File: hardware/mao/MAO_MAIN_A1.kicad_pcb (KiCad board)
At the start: 4 copper layers, 58 x 56 mm, 137 parts, among them J101 USB-C, J102 BAT, J201 TAG, J301 LCD, J501 LRA, Q101 AO3401A, Q302 DMG2302UK, Q501 AO3400A, SW301 SKQGADE010, U101 TPD2E2U06, U102 BQ25185DLHR, U103 MAX17048G+T10, U104 TPS62840DLCR, U105 TPS22916CYFPR, U201 ESP32-S3-MINI-1-N8, U301 DRV5012AEDMRR, U302 DRV5012AEDMRR, U304 TLV9061IDBVR, U401 ICM-42670-P, U402 VL53L4CDV0DH/1, U501 MAX98357AETE+T, U502 DRV2605LDGSR, U503 IRM-H638T/TR2, U504 TPS22916CYFPR

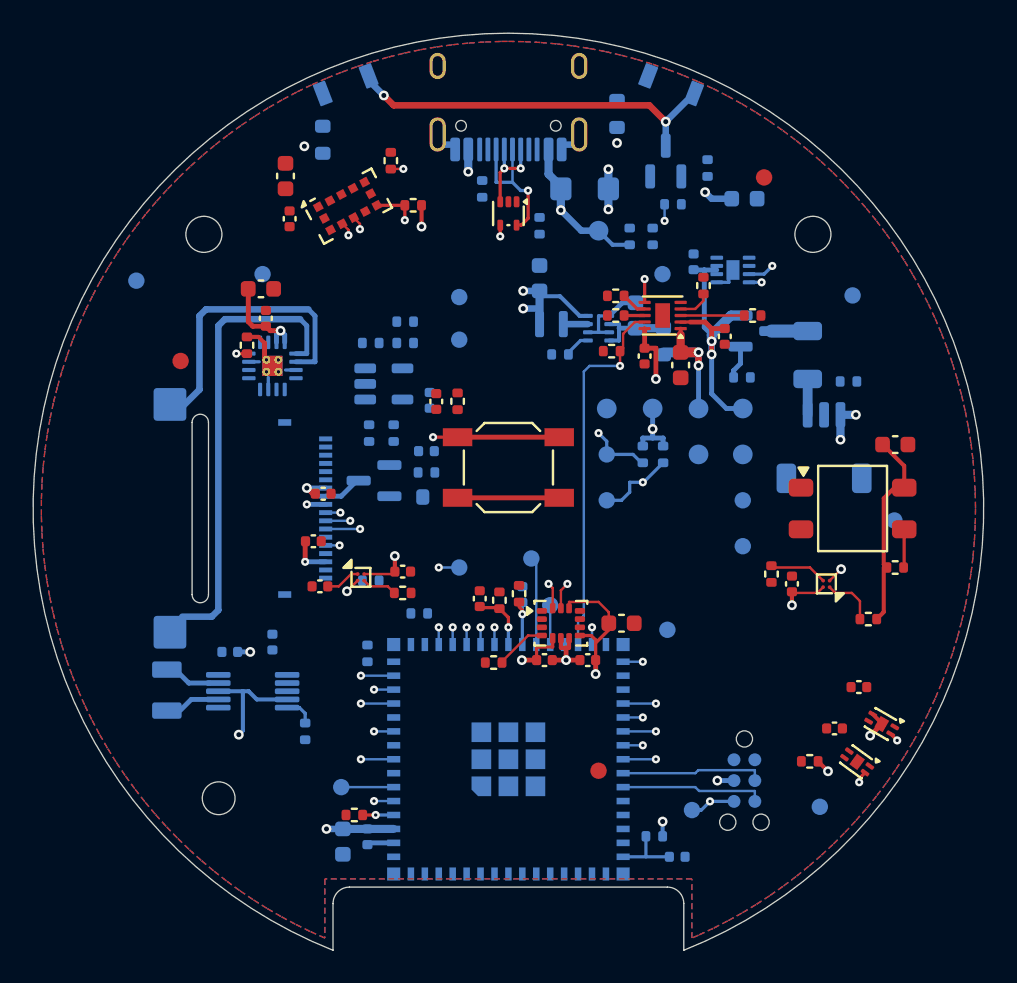
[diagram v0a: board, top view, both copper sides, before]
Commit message: A1 routed: DRC 0 / unconnected 0 / parity 0, planes continuous, silk/mech/stack-up checks clean, fab package
- Board: grid-router pass 10 (79 of 80 nets) + route_finish (AMP_LRCLK, four boxed GND pads incl. R117.2's
  pour island) + prune/stitch/tidy/offpad/snap45. kicad-cli DRC: 0 violations, 0 unconnected, 0 parity;
  plane_check: GND, VBUS, VSYS, +3V3 one piece each; ERC 0 (98 fitted + 5 DNP, 75 nets).
- silk.py / mao_labels.py: relaunch with subprocess instead of os.execv (Windows split the KiCad python path at
  its space and the silk pass silently did nothing); face identity moved to 3 o'clock (A1's escape vias took
  A0's spot), IMU axes scan for the nearest clear field, the back mark leaves the battery pin cues room.
  check_silk_text: 74 texts, 0 findings. mech_check: 137 parts, 0 findings.
- C402 fields synced to the Basic 10 nF part (sync_fields), schematic regenerated.
- outputs/fab: gerbers (12) + drill (4) + zip, JLC BOM 47 lines / 98 parts with sourcing columns, off-board
  LCSC list, CPL 98 rows, assembly drawings; layer plots and renders in docs/hardware.

Co-Authored-By: Claude Opus 5.5 <noreply@anthropic.com>
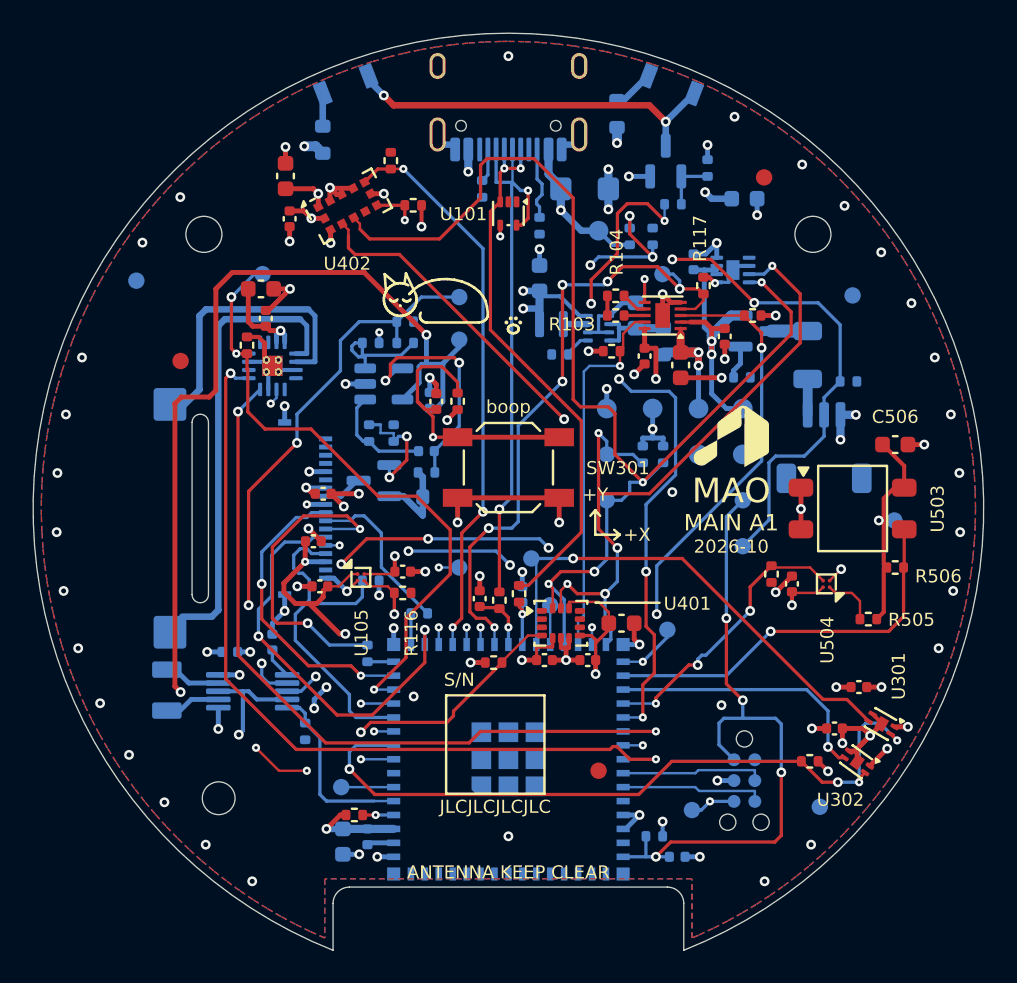
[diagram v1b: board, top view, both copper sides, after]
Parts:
- C402: value 10nF 16V -> 10nF 50V
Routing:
- net I2C_SDA: track 7.96 -> 100.1 mm, vias 4 -> 8
- net I2C_SCL: track 8.06 -> 97.4 mm, vias 4 -> 9
- net 3V3_LCD: track 4.53 -> 80.6 mm, vias 1 -> 6
- net GND: track 42.5 -> 116.2 mm, vias 13 -> 87
- net AMP_LRCLK: track 1.20 -> 60.7 mm, vias 1 -> 4
- net AMP_DIN: track 2.00 -> 50.4 mm, vias 1 -> 2
- net AMP_BCLK: track 2.00 -> 46.8 mm, vias 1 -> 2
- net HALL_FAST: track 1.29 -> 44.4 mm, vias 2 -> 4
- net LCD_BL: track 2.00 -> 43.9 mm, vias 1 -> 3
- net VBUS_SENSE: track 1.20 -> 42.8 mm, vias 1 -> 6
- net AMP_SD: track 2.61 -> 39.3 mm, vias 2 -> 3
- net CHG_CE_N: track 3.06 -> 39.5 mm, vias 1 -> 6
- net MCU_EN: track 4.07 -> 40.2 mm, vias 0 -> 4
- net IR_TX: track 2.06 -> 34.8 mm, vias 2 -> 3
- net TOF_XSHUT: track 1.82 -> 34.5 mm, vias 2 -> 3
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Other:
- board text added: "+X"
- board text added: "+Y"
- board text added: "- T + BAT"
- board text added: "2026-10"
- board text added: "3V3"
- board text added: "9 lives"
- board text added: "AMP"
- board text added: "ANTENNA KEEP CLEAR"
- board text added: "BAT"
- board text added: "BAT LINK"
- board text added: "BL"
- board text added: "BOOT"
- board text added: "CE"
- board text added: "GND"
- board text added: "HLA"
- board text added: "IO2"
- board text added: "IO26"
- board text added: "IRV"
- board text added: "JLCJLCJLCJLC"
- board text added: "LCD"
- board text added: "LCDV"
- board text added: "LRA"
- board text added: "MAIN A1"
- board text added: "MAO"
- board text added: "MAO A1"
- board text added: "PRS"
- board text added: "RST"
- board text added: "S/N"
- board text added: "SCL"
- board text added: "SDA"
- board text added: "SPK"
- board text added: "SYS"
- board text added: "TAG"
- board text added: "TE"
- board text added: "TSMR"
- board text added: "USB"
- board text added: "VBUS"
- board text added: "boop"
- board text added: "meow"

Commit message: A1 BOM (design review 2026-10-06): charger IN/BAT 2.2 uF 25 V 0402, DRV2605LDGST, DMG2302UKQ-7; backlight reference 95.8 mV -> 29.0 mA
C101/C103 move from 1 uF to 2.2 uF 25 V 0402 (CL05A225KA5NUNC, C307418) so at least 1 uF remains under DC bias
(TI SLUSF65B 7.2.2.3). DRV2605LDGSR -> DRV2605LDGST (C425927, same part, 250 reel) and DMG2302UK-7 -> DMG2302UKQ-7
(C5224573, same pinout) for stock. Fixes the backlight arithmetic in the capture notes (N7).

Co-Authored-By: Claude Opus 5.5 <noreply@anthropic.com>
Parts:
- C101, C103: value 1uF 25V -> 2.2uF 25V
- Q302: value DMG2302UK -> DMG2302UKQ
- U502: value DRV2605LDGSR -> DRV2605LDGST
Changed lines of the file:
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@@
 			)
 		)
-		(property "Value" "1uF 25V"
+		(property "Value" "2.2uF 25V"
 			(at 0 1.16 270)
 			(layer "F.Fab")
@@
 			)
 		)
-		(property "Description" "charger BAT (TI: >= 1 uF)"
+		(property "Description" "charger BAT: 2.2 uF 25 V 0402 keeps >= 1 uF at 4.2 V DC bias (SLUSF65B 7.2.2.3)"
 			(at 0 0 270)
 			(layer "F.Fab")
@@
 			)
 		)
-		(property "MPN" "CL05A105KA5NQNC"
+		(property "MPN" "CL05A225KA5NUNC"
 			(at 0 0 270)
 			(layer "F.Fab")
@@
 			)
 		)
-		(property "LCSC" "C52923"
+		(property "LCSC" "C307418"
 			(at 0 0 270)
 			(layer "F.Fab")
@@
 			)
 		)
-		(property "Value" "1uF 25V"
+		(property "Value" "2.2uF 25V"
 			(at 0 1.16 270)
 			(layer "F.Fab")
@@
 			)
 		)
-		(property "Description" "charger IN (TI: 1 uF, 25 V rating)"
+		(property "Description" "charger IN: 2.2 uF 25 V 0402 keeps >= 1 uF at 5 V DC bias (SLUSF65B 7.2.2.3)"
 			(at 0 0 270)
 			(layer "F.Fab")
@@
 			)
 		)
-		(property "MPN" "CL05A105KA5NQNC"
+		(property "MPN" "CL05A225KA5NUNC"
 			(at 0 0 270)
 			(layer "F.Fab")
@@
 			)
 		)
-		(property "LCSC" "C52923"
+		(property "LCSC" "C307418"
 			(at 0 0 270)
 			(layer "F.Fab")
@@
 			)
 		)
-		(property "Description" "reference divider top: 3.2 V -> 94.6 mV"
+		(property "Description" "reference divider top: 3.2 V x 1.0 / 33.4 = 95.8 mV"
 			(at 0 0 180)
 			(layer "B.Fab")
@@
 			)
 		)
-		(property "Value" "DMG2302UK"
+		(property "Value" "DMG2302UKQ"
 			(at 0 -2.4 0)
 			(layer "B.Fab")
@@
 			)
 		)
-		(property "Description" "backlight sink FET (pins 1 G, 2 S, 3 D)"
+		(property "Description" "backlight sink FET (pins 1 G, 2 S, 3 D); DMG2302UKQ-7 = the automotive-qualified DMG2302UK, same pinout"
 			(at 0 0 0)
 			(layer "B.Fab")
@@
 			)
 		)
-		(property "MPN" "DMG2302UK-7"
+		(property "MPN" "DMG2302UKQ-7"
 			(at 0 0 0)
 			(layer "B.Fab")
@@
 			)
 		)
-		(property "LCSC" "C460977"
+		(property "LCSC" "C5224573"
 			(at 0 0 0)
 			(layer "B.Fab")
@@
 			)
 		)
-		(property "Description" "Rs: 94.6 mV / 3.3 ohm = 28.7 mA LED current"
+		(property "Description" "Rs: 95.8 mV / 3.3 ohm = 29.0 mA LED current"
 			(at 0 0 180)
 			(layer "B.Fab")
@@
 			)
 		)
-		(property "Value" "DRV2605LDGSR"
+		(property "Value" "DRV2605LDGST"
 			(at 0 -2.45 0)
 			(layer "B.Fab")
@@
 			)
 		)
-		(property "Description" "haptic driver, auto-resonance"
+		(property "Description" "haptic driver, auto-resonance (DGST: the DGSR part on a 250-piece reel)"
 			(at 0 0 0)
 			(layer "B.Fab")
@@
 			)
 		)
-		(property "MPN" "DRV2605LDGSR"
+		(property "MPN" "DRV2605LDGST"
 			(at 0 0 0)
 			(layer "B.Fab")
@@
 			)
 		)
-		(property "LCSC" "C527464"
+		(property "LCSC" "C425927"
 			(at 0 0 0)
 			(layer "B.Fab")

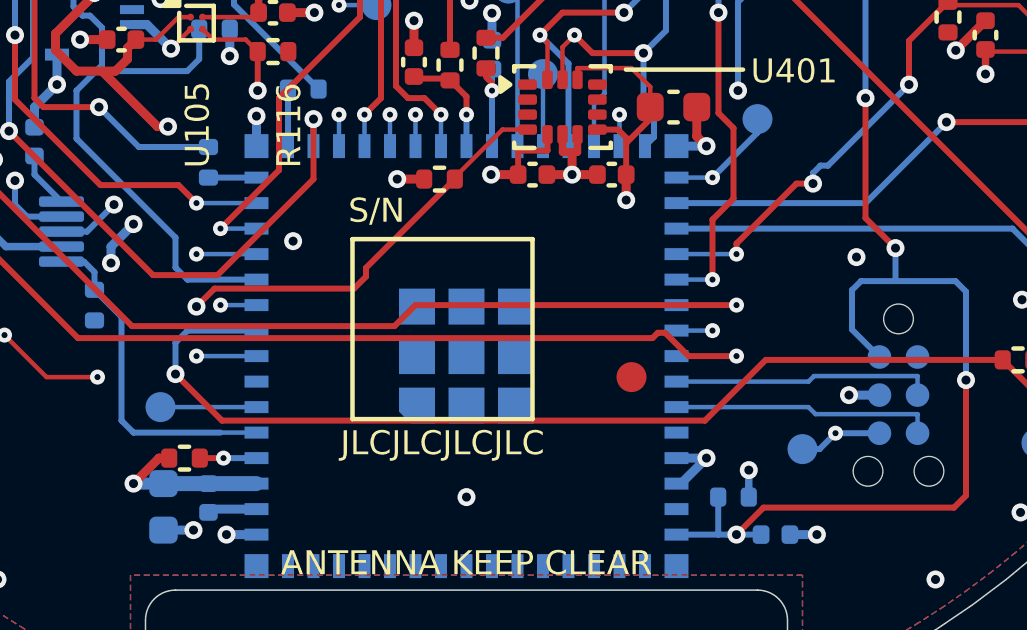
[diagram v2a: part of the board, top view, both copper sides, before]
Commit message: A1: USB wakes from deep sleep (design review 2026-10-06, finding 1)
VBUS_SENSE (GPIO39) is not an RTC pad. The 100k/150k VBUS divider now drives a 2N7002 (Q102, C8545 Basic) whose
drain, USB_PRESENT_N (100k pull-up R123, 33 uA only while USB is present), sits on the spare RTC pad GPIO2: an ext1
any-low wake source. GPIO39 is a spare with test pad TP26; TP24 now probes USB_PRESENT_N.

Layout (surgical, route_review.py): Q102/R123 on F east of the module's right escape column, gate on the router's
VBUS_SENSE line, drain down to an L3 run under the module (south of AMP_LRCLK) to GPIO2's stub; sync_fields.py --add
puts parts new in circuit.py on the routed board. DRC 0 / unconnected 0 / parity 0, planes continuous.

Firmware: MAO_LINE_USB_PRESENT reads GPIO2 active low, USB_PRESENT_N joins the A1 ext1 any-low mask when it idles
high (deep_sleep_hold and the critical sleep ask for it); MAO still never deep-sleeps with USB present.

Co-Authored-By: Claude Opus 5.5 <noreply@anthropic.com>
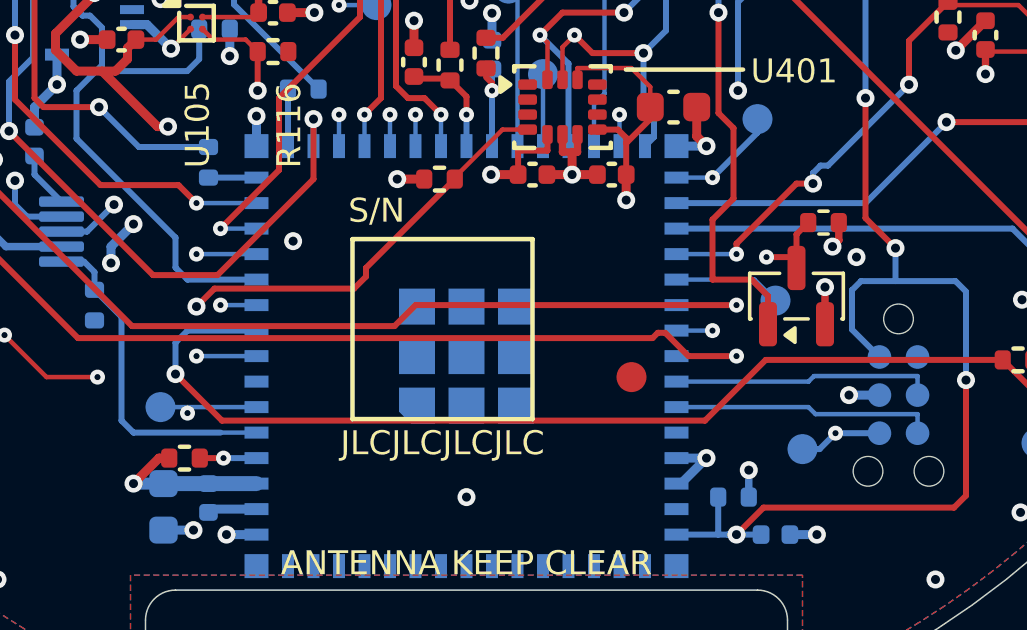
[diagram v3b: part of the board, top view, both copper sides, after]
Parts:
- added Q102: 2N7002, Package_TO_SOT_SMD:SOT-23, F.Cu at (61.0, 63.3)
- added R123: 100k, Resistor_SMD:R_0402_1005Metric, F.Cu at (61.9, 60.9)
- added TP26: IO39, TestPoint:TestPoint_Pad_D1.0mm, B.Cu at (60.3, 63.5)
- TP24: value IO2 -> USB
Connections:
- net GPIO2 renamed USB_PRESENT_N
- U201 pad 35: VBUS_SENSE -> GPIO39
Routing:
- net USB_PRESENT_N: track 3.20 -> 30.1 mm, vias 0 -> 2
- net GPIO39: track 0.00 -> 3.59 mm
- net VBUS_SENSE: track 42.8 -> 44.7 mm, vias 6 -> 5
- net GND: track 116.2 -> 117.5 mm, vias 87 -> 88
- net +3V3: track 53.1 -> 54.0 mm, vias 25 -> 26

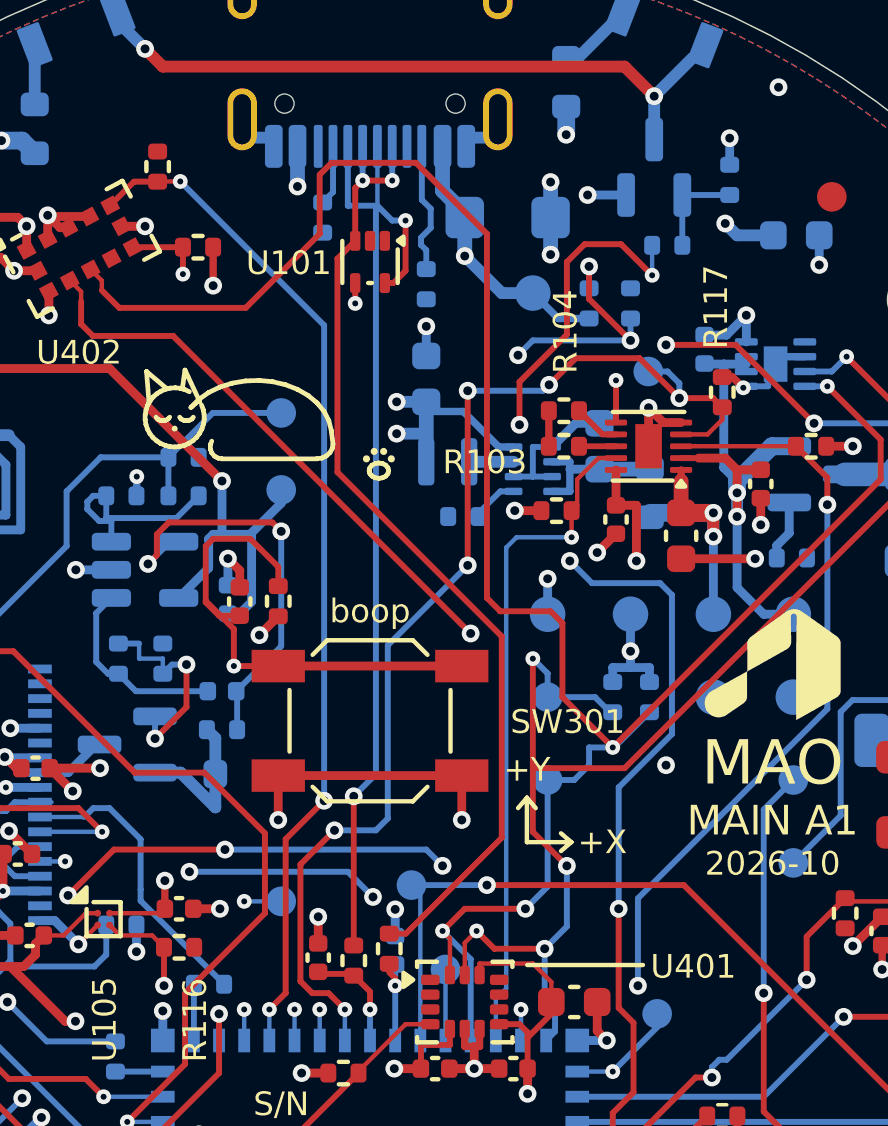
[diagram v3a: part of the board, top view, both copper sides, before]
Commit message: A1: USB D+/D- as one pair on F over the L2 ground (design review 2026-10-06, finding 3)
The router had D+ on F but D- down B (x 0.2) across the L3 VBUS / +3V3 split under the receptacle. Both lines now run
on F as a designed edge-coupled pair, w 0.15 / gap 0.25 (~90 ohm differential on JLC04161H-1080; project.py), from
the receptacle's F join / one D- via, in line through the ESD array (its two identical channels swap: pin 3 D-,
pin 5 D+), round the face switch's east side and into the 22R R216/R215 (route_local.USB_PAIR). To make room the I2C
data line turns 0.35 mm earlier and the I2C clock's B->L3 via north of the 22R moves 0.9 mm (route_review.py 3).
Pair: D+ 34.4 mm F + 1.1 mm B (contact stubs), D- 31.7 mm F + 3.9 mm B. DRC 0 / 0 / 0, planes continuous.

Co-Authored-By: Claude Opus 5.5 <noreply@anthropic.com>
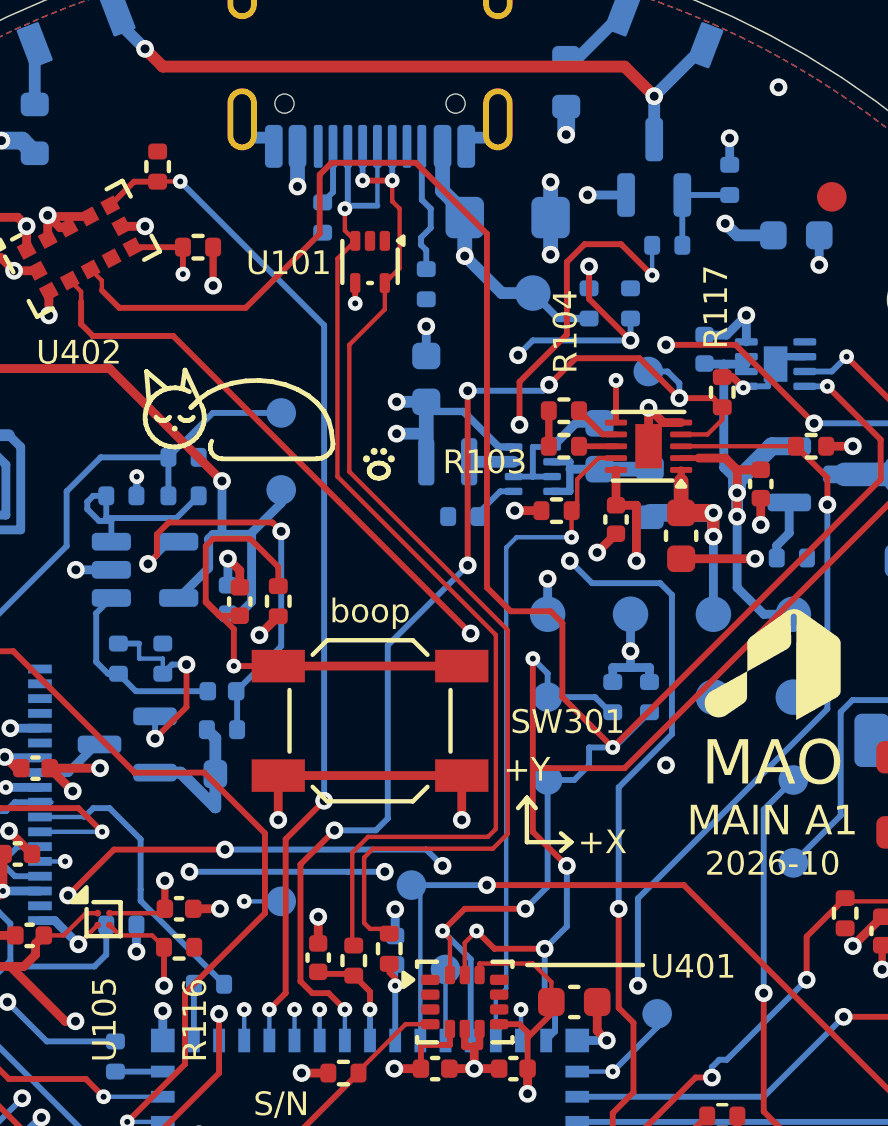
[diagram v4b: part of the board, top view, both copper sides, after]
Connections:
- U101 pad 3: USB_C_DP -> USB_C_DN
- U101 pad 5: USB_C_DN -> USB_C_DP
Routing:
- net USB_C_DP: track 32.1 -> 35.5 mm
- net USB_C_DN: track 32.8 -> 35.7 mm, vias 2 -> 1
- net I2C_SCL: track 97.4 -> 98.4 mm
